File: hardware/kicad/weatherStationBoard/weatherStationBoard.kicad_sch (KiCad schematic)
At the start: 51 parts, among them J1 USB_C_Receptacle_USB2.0_16P, J3 Conn_01x30_Pin, Q1 S8050, Q2 S8050, U1 ESP-12F, U2 CH340G, U3 BME680, U4 AMS1117-3.3, Y1 Crystal_GND24_Small

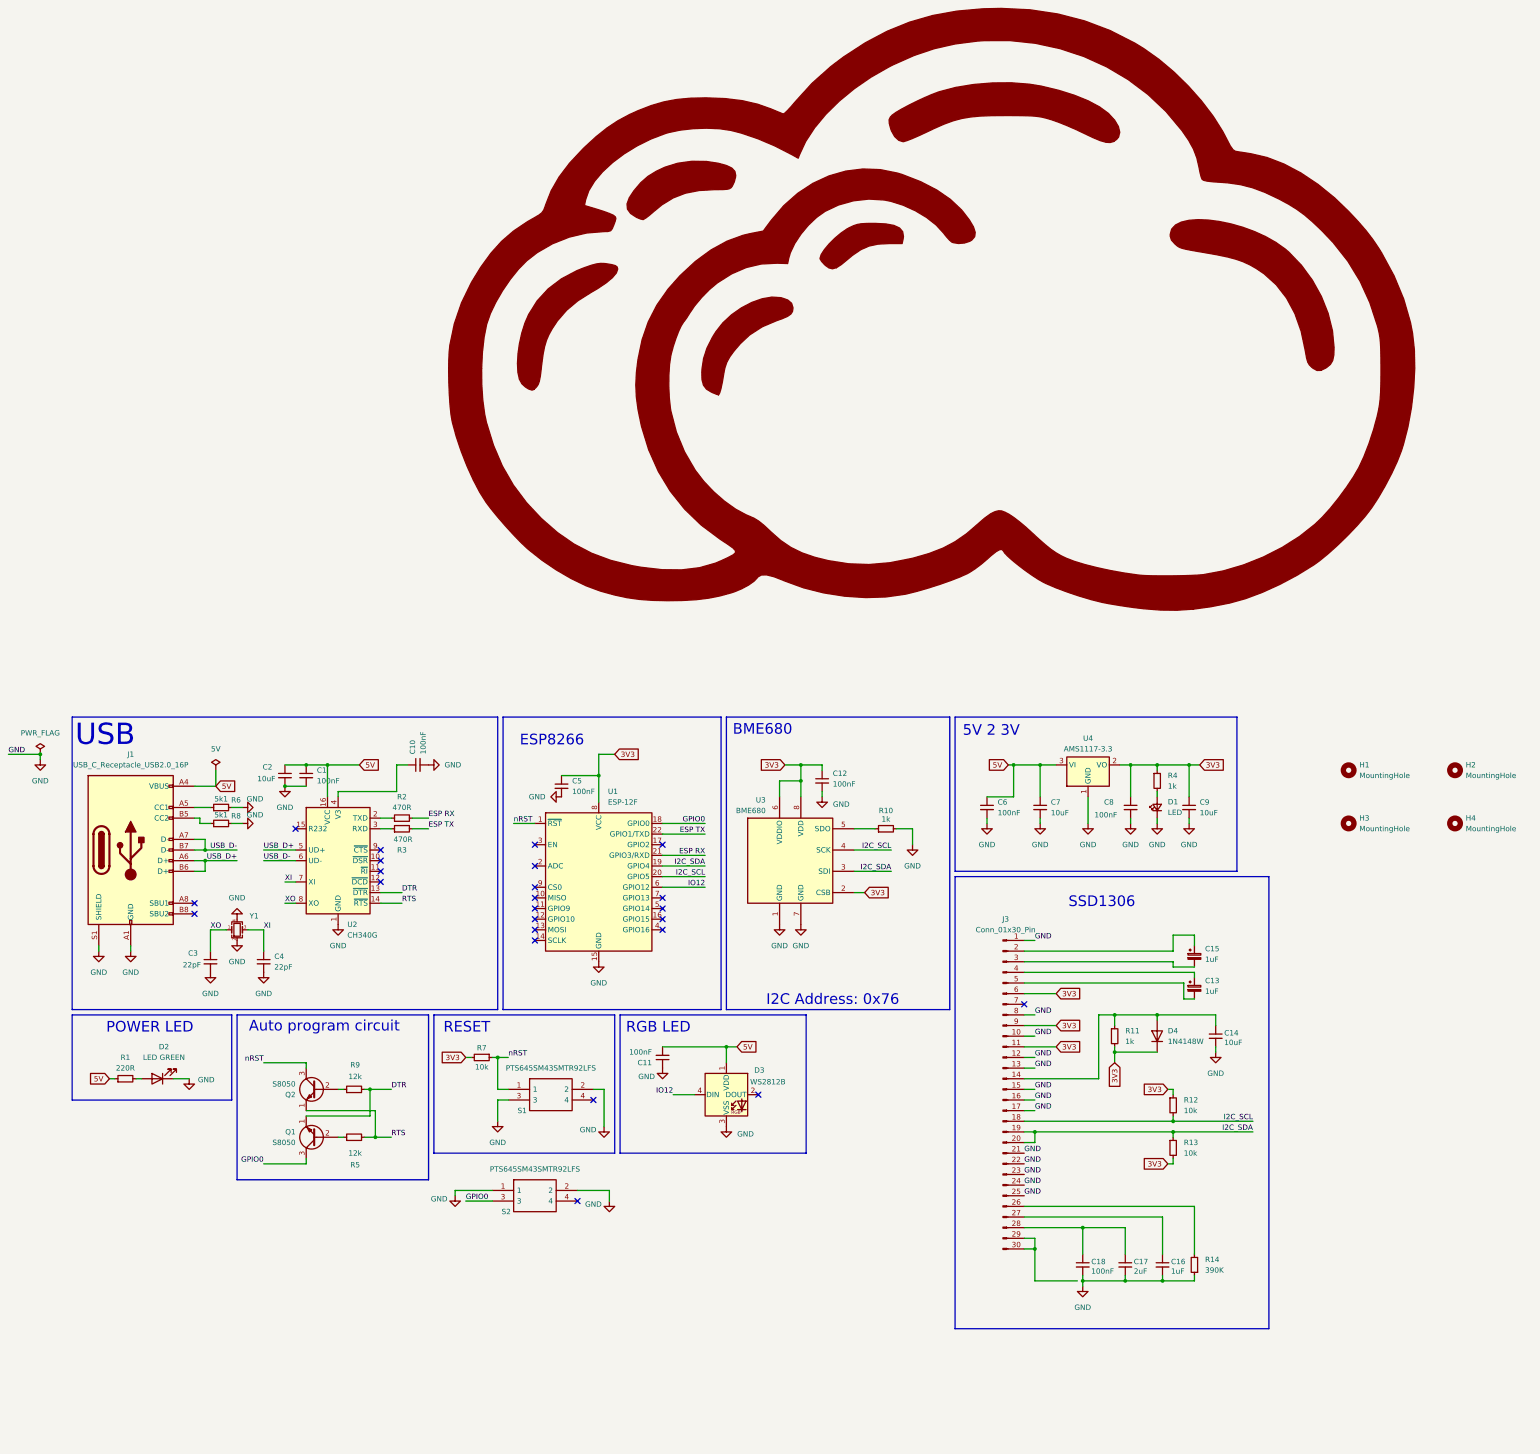
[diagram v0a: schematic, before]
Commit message: Testpoints added
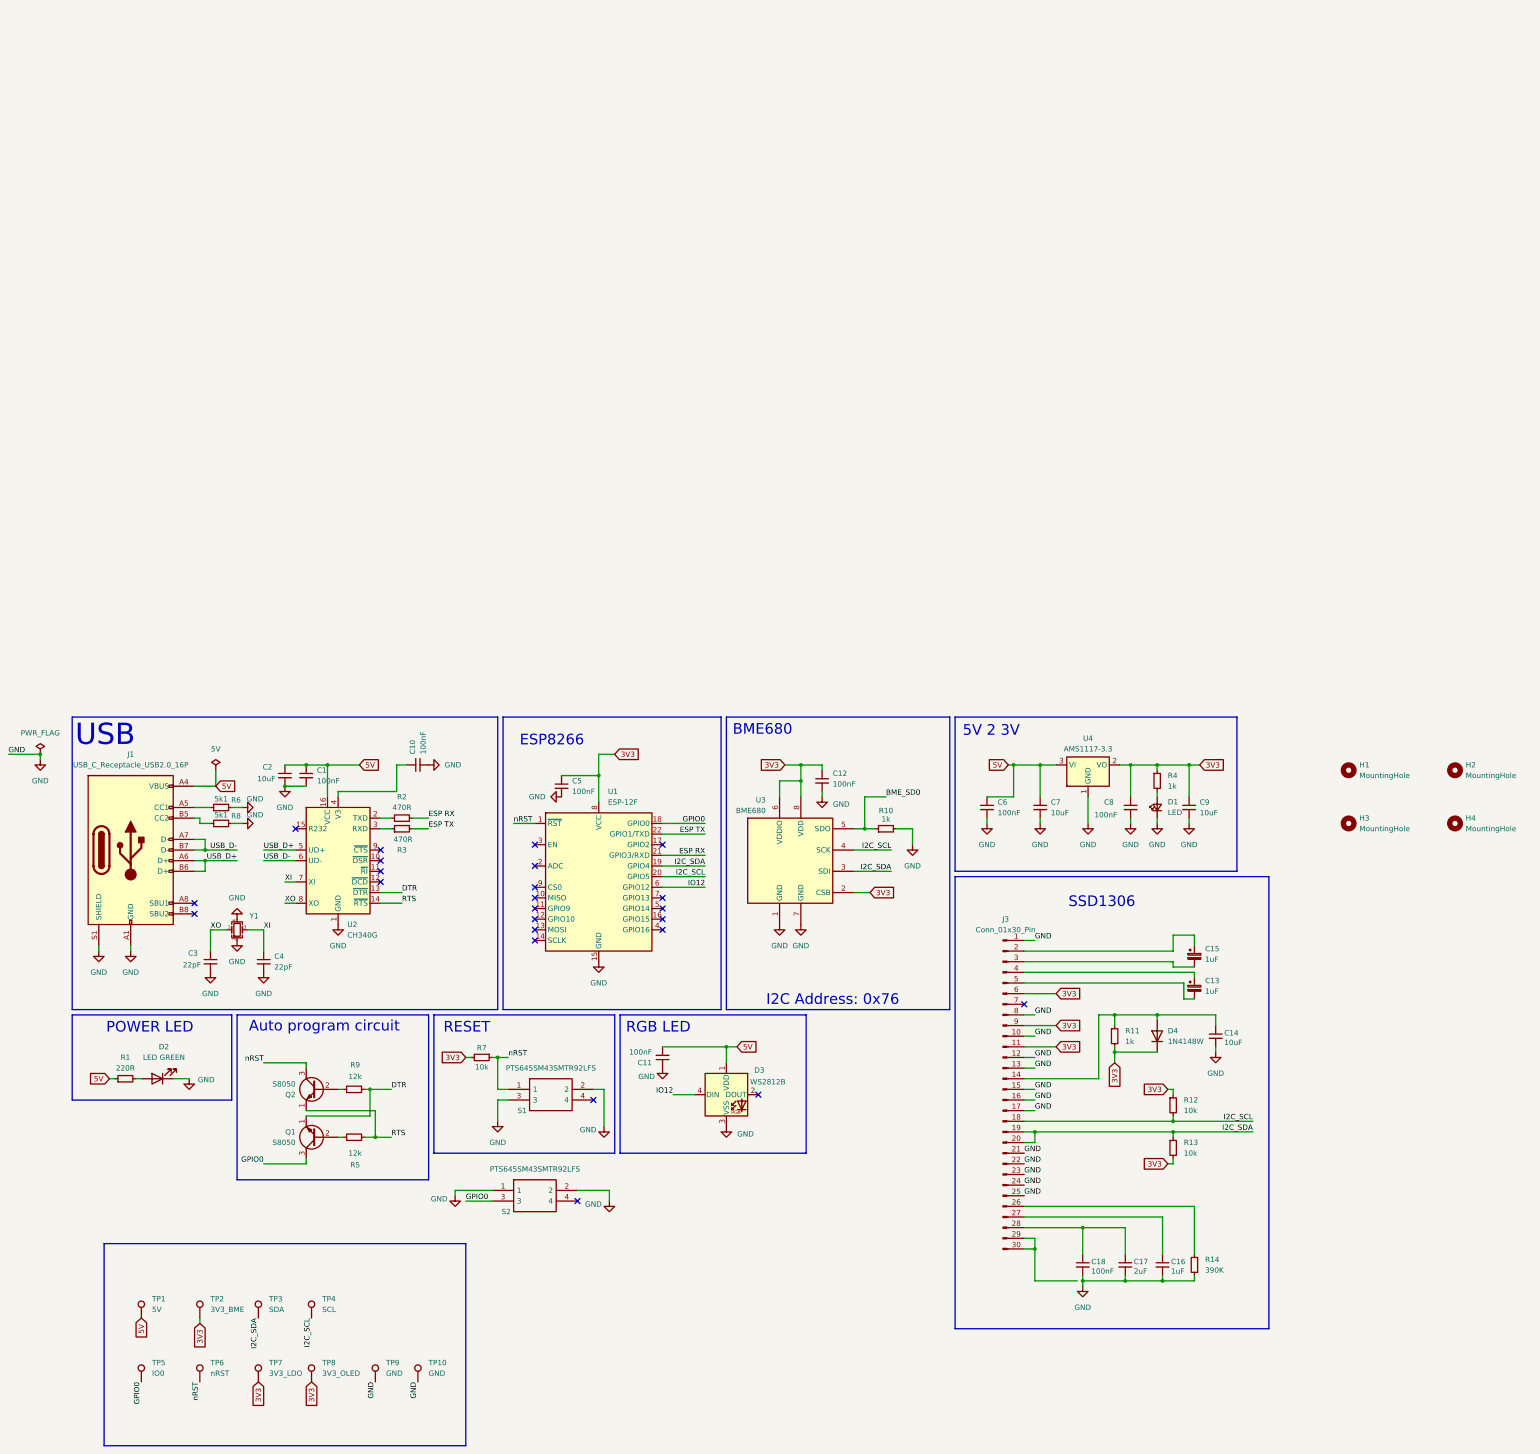
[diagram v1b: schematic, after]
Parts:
- added TP1: 5V, TestPoint:TestPoint_Pad_D1.0mm, symbol Connector:TestPoint
- added TP10, TP9: GND, TestPoint:TestPoint_Pad_D1.0mm, symbol Connector:TestPoint
- added TP2: 3V3_BME, TestPoint:TestPoint_Pad_D1.0mm, symbol Connector:TestPoint
- added TP3: SDA, TestPoint:TestPoint_Pad_D1.0mm, symbol Connector:TestPoint
- added TP4: SCL, TestPoint:TestPoint_Pad_D1.0mm, symbol Connector:TestPoint
- added TP5: IO0, TestPoint:TestPoint_Pad_D1.0mm, symbol Connector:TestPoint
- added TP6: nRST, TestPoint:TestPoint_Pad_D1.0mm, symbol Connector:TestPoint
- added TP7: 3V3_LDO, TestPoint:TestPoint_Pad_D1.0mm, symbol Connector:TestPoint
- added TP8: 3V3_OLED, TestPoint:TestPoint_Pad_D1.0mm, symbol Connector:TestPoint
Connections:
- net 3V3: now also TP2.1, TP7.1, TP8.1
- net 5V: now also TP1.1
- net GND: now also TP10.1, TP9.1
- net GPIO0: now also TP5.1
- net I2C_SCL: now also TP4.1
- net I2C_SDA: now also TP3.1
- net nRST: now also TP6.1
- net BME_SD0: now reaches R10.1, U3.5 (SDO)

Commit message: REV1 WeatherStationBoard
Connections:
- net GND: now also J3.29 (Pin_29), J3.30 (Pin_30)
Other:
- note added: "AMS1117 5V TO 3V3"
- note removed: "5V 2 3V"
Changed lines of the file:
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@@
 	(wire
 		(pts
+			(xy 73.66 21.59) (xy 73.66 24.13)
+		)
+		(stroke
+			(width 0)
+			(type default)
+		)
+	)
+	(wire
+		(pts
 			(xy 86.36 54.61) (xy 91.44 54.61)
 		)
@@
 	(wire
 		(pts
-			(xy 73.66 24.13) (xy 81.28 24.13)
-		)
-		(stroke
-			(width 0)
-			(type default)
-		)
-	)
-	(wire
-		(pts
 			(xy 93.98 36.83) (xy 97.79 36.83)
 		)
@@
 	(wire
 		(pts
-			(xy 242.57 147.32) (xy 252.73 147.32)
+			(xy 242.57 147.32) (xy 254 147.32)
 		)
 		(stroke
@@
 		)
 	)
-	(text "5V 2 3V"
+	(text "AMS1117 5V TO 3V3"
 		(exclude_from_sim no)
-		(at 232.156 16.002 0)
+		(at 243.84 16.002 0)
 		(effects
 			(font
@@
 	(global_label "5V"
 		(shape input)
-		(at 81.28 24.13 0)
+		(at 73.66 21.59 90)
 		(fields_autoplaced yes)
 		(effects
@@
 		)
 		(property "Intersheetrefs" "${INTERSHEET_REFS}"
-			(at 86.5633 24.13 0)
+			(at 73.66 16.3067 90)
 			(effects
 				(font
@@
 		(dnp no)
 		(property "Reference" "C1"
-			(at 71.12 25.4062 0)
+			(at 67.31 22.352 0)
 			(effects
 				(font
@@
 		)
 		(property "Value" "100nF"
-			(at 71.12 27.9462 0)
+			(at 65.532 20.32 0)
 			(effects
 				(font
